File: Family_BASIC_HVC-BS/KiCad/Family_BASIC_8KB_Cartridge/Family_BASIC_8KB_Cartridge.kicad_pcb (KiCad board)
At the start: 2 copper layers, 90 x 90 mm, 21 parts, among them IC1 Working RAM (62256), IC3 74HCT20, IC4 Character ROM (2764), SW1 BACKUP SW, SW2 RAM BANK SW, SW3 A_{15} SW, U1 Program ROM (27512)

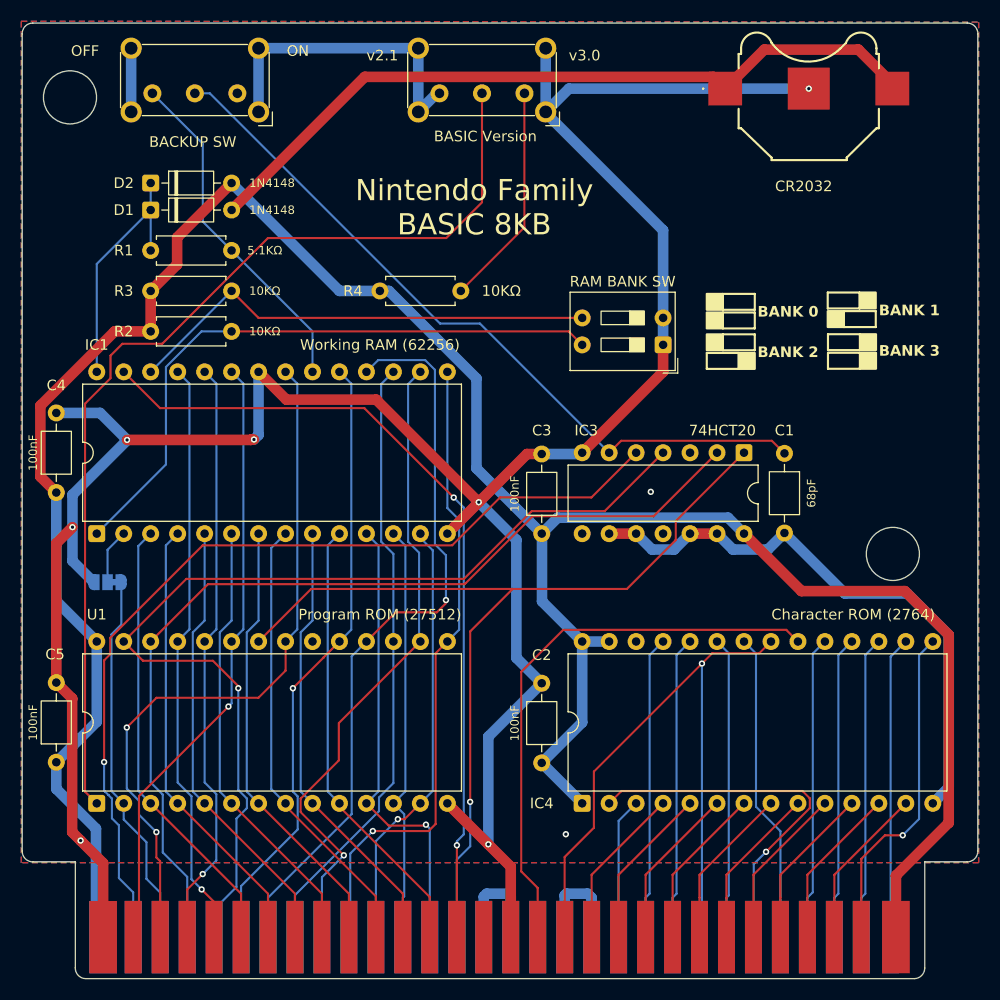
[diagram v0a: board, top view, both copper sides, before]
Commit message: Reorganised KiCad folders
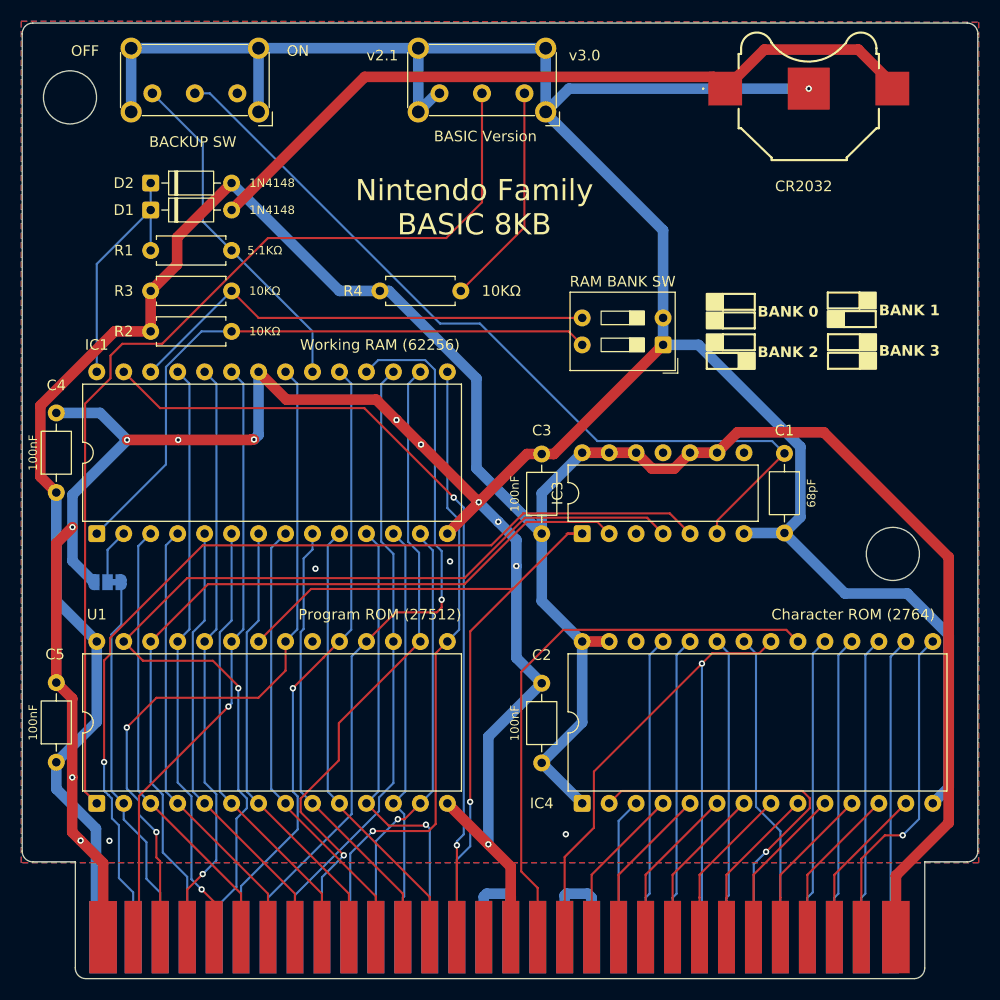
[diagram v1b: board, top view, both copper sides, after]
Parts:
- moved IC3 17.0 mm to (110.8, 105.6), turned to 90 degrees
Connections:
- IC3 pad 10: /GND -> /V_{CC}
- IC3 pad 12: /GND -> /V_{CC}
- IC3 pad 13: /GND -> /V_{CC}
- IC3 pad 9: /GND -> /V_{CC}
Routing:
- net /GND: track 339.4 -> 372.4 mm, vias 9 -> 17
- net /~{ROMSEL}: track 89.5 -> 71.5 mm
- net /V_{CC}: track 241.7 -> 256.1 mm
- net /A_{13}: track 90.0 -> 77.6 mm
- net Net-(SW1-B): track 70.5 -> 79.8 mm
- net /O2: track 86.3 -> 89.8 mm
- net /A_{14}: track 95.9 -> 94.0 mm
